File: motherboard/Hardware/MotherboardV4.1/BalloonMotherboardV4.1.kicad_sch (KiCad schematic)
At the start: 5 parts

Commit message: changed opamp
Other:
- note added: "Bekannte Designfehler - keine seperate Analog/HF Groundplanes - no ESD Protection"
- note added: "optional Upgrades - USB-PD - replace LDOs with low noise buck converter"
- note removed: "Bekannte Designfehler - Input Rush von Buck Converter Condesnsatoren von Heater Condensatoren nicht begrenzt (induktor?) - Voltageshifter OE uC controlled + pulldown resistor - keine seperate Analog/HF Groundplanes - no ESD Protection - Rework OPamp choice - change current sensing to lowside and add capasitance"
- note removed: "optional Upgrades - MUX Serial communication for Oxygen Sensors - USB-PD - dedicated current sense amplifier - Battery Voltage Measurement before shunt - replace LDOs with low noise buck converter"
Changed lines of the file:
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@@
 		)
 	)
-	(text "optional Upgrades\n- MUX Serial communication for Oxygen Sensors\n- USB-PD\n- dedicated current sense amplifier\n- Battery Voltage Measurement before shunt\n- replace LDOs with low noise buck converter\n"
+	(text "optional Upgrades\n- USB-PD\n- replace LDOs with low noise buck converter\n"
 		(exclude_from_sim no)
-		(at 185.42 123.952 0)
+		(at 185.42 98.298 0)
 		(effects
 			(font
@@
 		)
 	)
-	(text "Bekannte Designfehler\n- Input Rush von Buck Converter Condesnsatoren \n		     von Heater Condensatoren\n	nicht begrenzt (induktor?)\n- Voltageshifter OE uC controlled + pulldown resistor\n- keine seperate Analog/HF Groundplanes\n- no ESD Protection\n- Rework OPamp choice\n- change current sensing to lowside and add capasitance"
+	(text "Bekannte Designfehler\n- keine seperate Analog/HF Groundplanes\n- no ESD Protection"
 		(exclude_from_sim no)
 		(at 185.674 77.724 0)

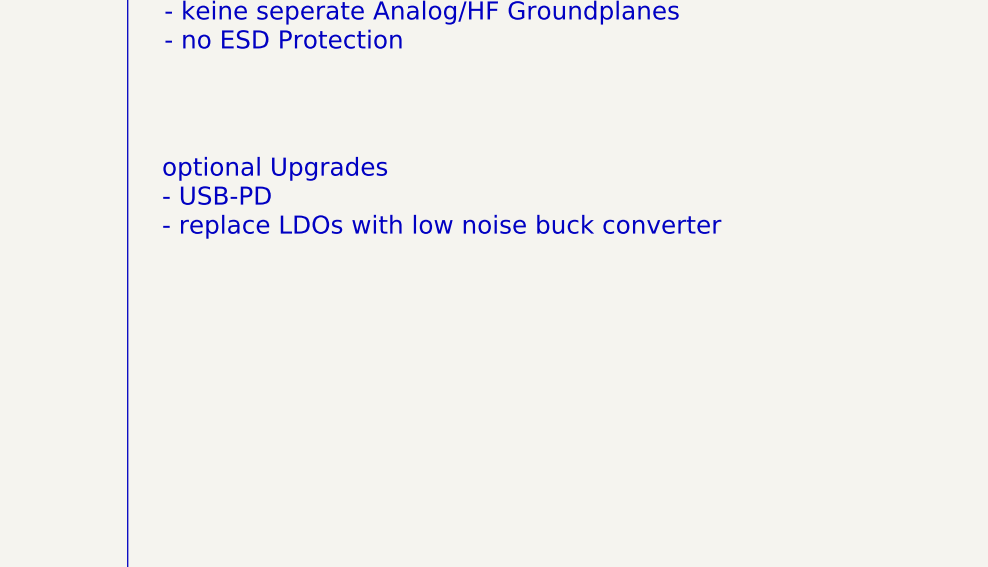
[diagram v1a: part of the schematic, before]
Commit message: refined thermal controller
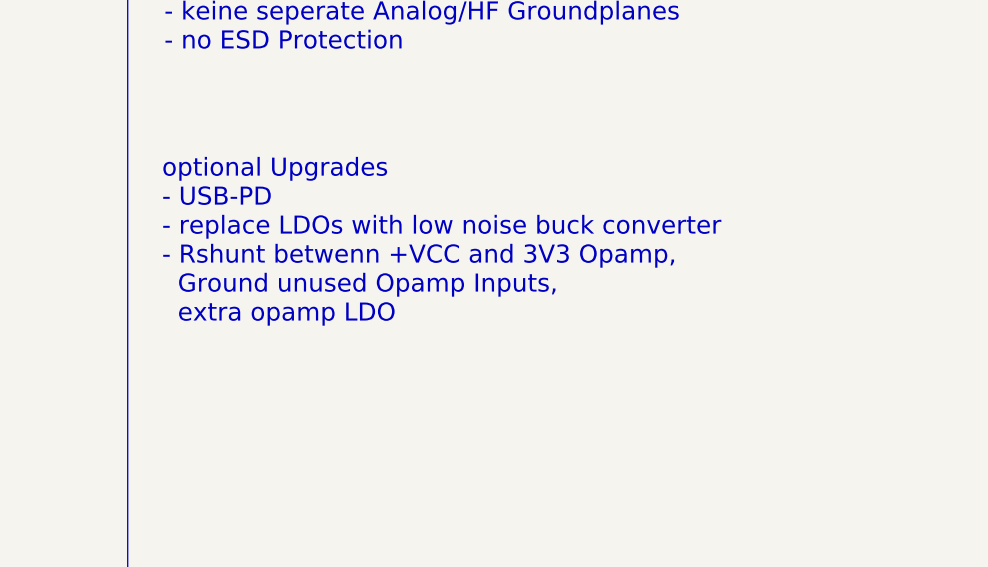
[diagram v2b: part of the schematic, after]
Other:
- note added: "optional Upgrades - USB-PD - replace LDOs with low noise buck converter - Rshunt betwenn +VCC and 3V3 Opamp, Ground unused Opamp Inputs, extra opamp LDO"
- note removed: "optional Upgrades - USB-PD - replace LDOs with low noise buck converter"
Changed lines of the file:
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@@
 		)
 	)
-	(text "optional Upgrades\n- USB-PD\n- replace LDOs with low noise buck converter\n"
+	(text "optional Upgrades\n- USB-PD\n- replace LDOs with low noise buck converter\n- Rshunt betwenn +VCC and 3V3 Opamp, \n  Ground unused Opamp Inputs,\n  extra opamp LDO\n"
 		(exclude_from_sim no)
 		(at 185.42 98.298 0)

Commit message: working on thermal
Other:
- note added: "Bekannte Designfehler - keine seperate Analog/HF Groundplanes - no ESD Protection - Buck Heat Condensators won't decharge if heater off - Inrush current limiting Resistor has to handle way to mutch power"
- note removed: "Bekannte Designfehler - keine seperate Analog/HF Groundplanes - no ESD Protection"
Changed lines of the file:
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@@
 		)
 	)
-	(text "Bekannte Designfehler\n- keine seperate Analog/HF Groundplanes\n- no ESD Protection"
+	(text "Bekannte Designfehler\n- keine seperate Analog/HF Groundplanes\n- no ESD Protection\n- Buck Heat Condensators won't decharge if heater off\n- Inrush current limiting Resistor has to handle way to mutch power"
 		(exclude_from_sim no)
 		(at 185.674 77.724 0)

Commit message: worked on thermals
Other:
- note added: "optional Upgrades - USB-PD - replace LDOs with low noise buck converter - Rshunt betwenn +VCC and 3V3 Opamp, Ground unused Opamp Inputs, extra opamp LDO - EMF Capasitor Switcher"
- note removed: "optional Upgrades - USB-PD - replace LDOs with low noise buck converter - Rshunt betwenn +VCC and 3V3 Opamp, Ground unused Opamp Inputs, extra opamp LDO"
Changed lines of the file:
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@@
 		)
 	)
-	(text "optional Upgrades\n- USB-PD\n- replace LDOs with low noise buck converter\n- Rshunt betwenn +VCC and 3V3 Opamp, \n  Ground unused Opamp Inputs,\n  extra opamp LDO\n"
+	(text "optional Upgrades\n- USB-PD\n- replace LDOs with low noise buck converter\n- Rshunt betwenn +VCC and 3V3 Opamp, \n  Ground unused Opamp Inputs,\n  extra opamp LDO\n- EMF Capasitor Switcher\n"
 		(exclude_from_sim no)
 		(at 185.42 98.298 0)
